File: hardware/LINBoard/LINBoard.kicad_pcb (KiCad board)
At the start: 2 copper layers, 22.6 x 12.4 mm, 10 parts, among them J1 Conn_01x02_Pin, SW1 SW_SPDT, U1 TLIN2029ADRQ1

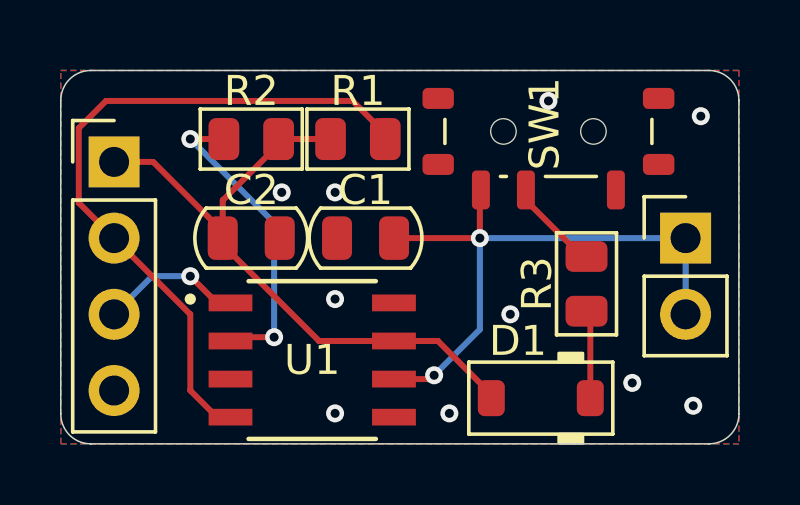
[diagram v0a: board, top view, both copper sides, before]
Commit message: Shrunk LINBoard.
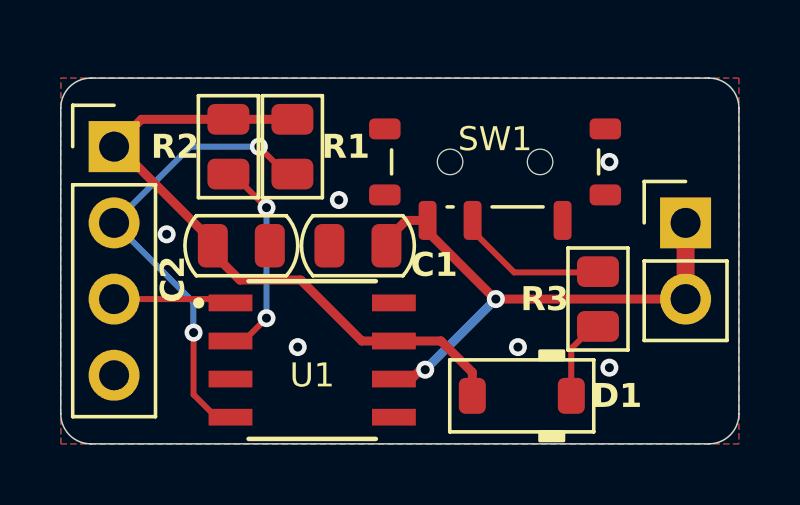
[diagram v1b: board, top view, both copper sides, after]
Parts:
- moved R1 2.20 mm to (84.7, 53.6), turned to -90 degrees
- moved SW1 2.05 mm to (91.4, 54.1)
- moved R2 0.80 mm to (82.5, 53.6), turned to -90 degrees
- moved D1 0.64 mm to (92.3, 61.9)
- moved R3 0.63 mm to (94.9, 58.7)
- moved J1 0.51 mm to (97.8, 56.1)
- moved J2 0.51 mm to (78.7, 53.6)
- moved C2 0.42 mm to (83.0, 56.9)
- moved C1 0.36 mm to (86.9, 56.9)
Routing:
- net Net-(J2-Pin_2): track 23.2 -> 15.8 mm, vias 0 -> 2
- net Net-(U1-EN): track 10.4 -> 6.93 mm
- net Net-(J1-Pin_1): track 20.9 -> 18.8 mm
- net Net-(SW1-B): track 3.14 -> 5.10 mm
- net Net-(J2-Pin_3): track 4.77 -> 3.93 mm, vias 1 -> 0
- net GNDREF: vias 10 -> 6
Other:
- board size 22.6 x 12.4 mm -> 22.6 x 12.2 mm

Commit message: Updated step files for all boards, footprints for LINBoard.
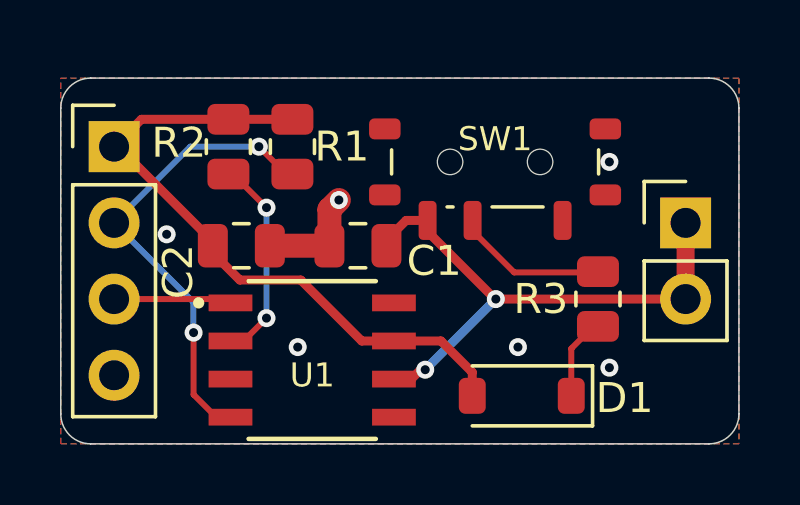
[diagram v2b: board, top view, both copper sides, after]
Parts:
- C1, C2: footprint PCM_Capacitor_SMD_AKL:C_0805_2012Metric -> Capacitor_SMD:C_0805_2012Metric
- D1: footprint PCM_Diode_SMD_AKL:D_SOD-123 -> Diode_SMD:D_SOD-123
- R1, R2, R3: footprint PCM_Resistor_SMD_AKL:R_0805_2012Metric -> Resistor_SMD:R_0805_2012Metric
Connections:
- SW1 pad SH: GNDREF -> (no net)
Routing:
- net GNDREF: track 0.00 -> 3.64 mm
